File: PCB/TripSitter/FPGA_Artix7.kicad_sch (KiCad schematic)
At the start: 31 parts, among them U1 XC7A100T-FGG484, U3 IS62WVS2568FBLL-20NLI

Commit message: attempt at routing
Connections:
- now unconnected: U1.A13 (IO_L10P_T1_16), U1.A14 (IO_L10N_T1_16), U1.A15 (IO_L9P_T1_DQS_16), U1.A16 (IO_L9N_T1_DQS_16), U1.A18 (IO_L17P_T2_16), U1.A19 (IO_L17N_T2_16), U1.A20 (IO_L16N_T2_16), U1.A21 (IO_L21N_T3_DQS_16), U1.B13 (IO_L8N_T1_16), U1.B15 (IO_L7P_T1_16), U1.B16 (IO_L7N_T1_16), U1.B17 (IO_L11P_T1_SRCC_16), U1.B18 (IO_L11N_T1_SRCC_16), U1.B20 (IO_L16P_T2_16), U1.B21 (IO_L21P_T3_DQS_16), U1.B22 (IO_L20N_T3_16), U1.C13 (IO_L8P_T1_16), U1.C17 (IO_L12N_T1_MRCC_16), U1.C18 (IO_L13P_T2_MRCC_16), U1.C19 (IO_L13N_T2_MRCC_16), U1.C20 (IO_L19N_T3_VREF_16), U1.C22 (IO_L20P_T3_16), U1.D15 (IO_L6N_T0_VREF_16), U1.D17 (IO_L12P_T1_MRCC_16), U1.D19 (IO_L14N_T2_SRCC_16), U1.D20 (IO_L19P_T3_16), U1.D21 (IO_L23N_T3_16), U1.D22 (IO_L22N_T3_16), U1.E18 (IO_L15N_T2_DQS_16), U1.E19 (IO_L14P_T2_SRCC_16), U1.E21 (IO_L23P_T3_16), U1.E22 (IO_L22P_T3_16), U1.F18 (IO_L15P_T2_DQS_16), U1.F19 (IO_L18P_T2_16), U1.F20 (IO_L18N_T2_16), U1.G21 (IO_L24P_T3_16), U1.G22 (IO_L24N_T3_16)
- no-connect marks 52 -> 87

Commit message: before
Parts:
- added J14: Conn_02x10_Counter_Clockwise, Connector_PinHeader_1.00mm:PinHeader_2x10_P1.00mm_Vertical, symbol Connector_Generic:Conn_02x10_Counter_Clockwise
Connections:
- net +3V3 is gone; now on net +3.3V: C28.1, C30.1, C31.1, C32.1, C33.1, C34.1, C35.1, C36.1, C37.1, C38.1, C39.1, C40.1, C41.1, C42.1, C43.1, C44.1, C45.1, C80.1, C81.1, C82.1, C83.1, C87.1, C88.1, C89.1, C90.1, C91.1, C92.1, C93.1, U1.A17 (VCCO_16), U1.AA17 (VCCO_13), U1.AB14 (VCCO_13), U1.B14 (VCCO_16), U1.C21 (VCCO_16), U1.D18 (VCCO_16), U1.E15 (VCCO_16), U1.F22 (VCCO_16), U1.G19 (VCCO_15), U1.H16 (VCCO_15), U1.J13 (VCCO_15), U1.K20 (VCCO_15), U1.L17 (VCCO_15), U1.M14 (VCCO_14), U1.N21 (VCCO_15), U1.P18 (VCCO_14), U1.R15 (VCCO_14), U1.T22 (VCCO_14), U1.U19 (VCCO_14), U1.V16 (VCCO_13), U1.W13 (VCCO_13), U1.Y10 (VCCO_13), U1.Y20 (VCCO_14)
- net at U1.AA10 (IO_L9P_T1_DQS_13): now also J14.7 (Pin_7)
- net at U1.AA11 (IO_L9N_T1_DQS_13): now also J14.8 (Pin_8)
- net at U1.AA9 (IO_L8P_T1_13): now also J14.5 (Pin_5)
- net at U1.AB10 (IO_L8N_T1_13): now also J14.6 (Pin_6)
- net at U1.AB11 (IO_L7P_T1_13): now also J14.3 (Pin_3)
- net at U1.AB12 (IO_L7N_T1_13): now also J14.4 (Pin_4)
- net FPGA_BANK13_20: now reaches U1.T14 (IO_L15P_T2_DQS_13)
- net FPGA_BANK13_20: now also J14.12 (Pin_12)
- net FPGA_BANK13_21: now reaches U1.T15 (IO_L15N_T2_DQS_13)
- net FPGA_BANK13_21: now also J14.11 (Pin_11)
- net FPGA_BANK13_18: now reaches U1.U15 (IO_L14P_T2_SRCC_13)
- net FPGA_BANK13_18: now also J14.14 (Pin_14)
- net at U1.V10 (IO_L10P_T1_13): now also J14.9 (Pin_9)
- net FPGA_BANK13_16: now reaches U1.V13 (IO_L13P_T2_MRCC_13)
- net FPGA_BANK13_16: now also J14.16 (Pin_16)
- net FPGA_BANK13_17: now reaches U1.V14 (IO_L13N_T2_MRCC_13)
- net FPGA_BANK13_17: now also J14.15 (Pin_15)
- net FPGA_BANK13_19: now reaches U1.V15 (IO_L14N_T2_SRCC_13)
- net FPGA_BANK13_19: now also J14.13 (Pin_13)
- net at U1.W10 (IO_L10N_T1_13): now also J14.10 (Pin_10)
- net FPGA_BANK13_15: now reaches U1.W11 (IO_L12P_T1_MRCC_13)
- net FPGA_BANK13_15: now also U1.W12 (IO_L12N_T1_MRCC_13), J14.17 (Pin_17), J14.18 (Pin_18)
- net at U1.W14 (IO_L6P_T0_13): now also J14.1 (Pin_1)
- net FPGA_BANK13_13: now reaches U1.Y11 (IO_L11P_T1_SRCC_13)
- net FPGA_BANK13_13: now also J14.20 (Pin_20)
- net FPGA_BANK13_14: now reaches U1.Y12 (IO_L11N_T1_SRCC_13)
- net FPGA_BANK13_14: now also J14.19 (Pin_19)
- net at U1.Y14 (IO_L6N_T0_VREF_13): now also J14.2 (Pin_2)
- net MCU_PE7: now reaches U1.L15 (IO_L22N_T3_A16_15)
- net EBI_A0: no longer names the net of U1.J16 (IO_0_15)
- net EBI_A1: no longer names the net of U1.H13 (IO_L1P_T0_AD0P_15)
- net EBI_A10: no longer names the net of U1.H15 (IO_L5N_T0_AD9N_15)
- net EBI_A11: no longer names the net of U1.H17 (IO_L6P_T0_15)
- net EBI_A12: no longer names the net of U1.H18 (IO_L6N_T0_VREF_15)
- net EBI_A13: no longer names the net of U1.J22 (IO_L7P_T1_AD2P_15)
- net EBI_A14: no longer names the net of U1.H22 (IO_L7N_T1_AD2N_15)
- net EBI_A15: no longer names the net of U1.H20 (IO_L8P_T1_AD10P_15)
- net EBI_A16: no longer names the net of U1.G20 (IO_L8N_T1_AD10N_15)
- net EBI_A17: no longer names the net of U1.K21 (IO_L9P_T1_DQS_AD3P_15)
- net EBI_A18: no longer names the net of U1.K22 (IO_L9N_T1_DQS_AD3N_15)
- net EBI_A19: no longer names the net of U1.M21 (IO_L10P_T1_AD11P_15)
- net EBI_A2: no longer names the net of U1.G13 (IO_L1N_T0_AD0N_15)
- net EBI_A20: no longer names the net of U1.L21 (IO_L10N_T1_AD11N_15)
- net EBI_A21: no longer names the net of U1.J20 (IO_L11P_T1_SRCC_15)
- net EBI_A22: no longer names the net of U1.J21 (IO_L11N_T1_SRCC_15)
- net EBI_A23: no longer names the net of U1.J19 (IO_L12P_T1_MRCC_15)
- net EBI_A24: no longer names the net of U1.H19 (IO_L12N_T1_MRCC_15)
- net EBI_A25: no longer names the net of U1.K18 (IO_L13P_T2_MRCC_15)
- net EBI_A26: no longer names the net of U1.K19 (IO_L13N_T2_MRCC_15)
- net EBI_A27: no longer names the net of U1.L19 (IO_L14P_T2_SRCC_15)
- net EBI_A3: no longer names the net of U1.G15 (IO_L2P_T0_AD8P_15)
- net EBI_A4: no longer names the net of U1.G16 (IO_L2N_T0_AD8N_15)
- net EBI_A5: no longer names the net of U1.J14 (IO_L3P_T0_DQS_AD1P_15)
- net EBI_A6: no longer names the net of U1.H14 (IO_L3N_T0_DQS_AD1N_15)
- net EBI_A7: no longer names the net of U1.G17 (IO_L4P_T0_15)
- net EBI_A8: no longer names the net of U1.G18 (IO_L4N_T0_15)
- net EBI_A9: no longer names the net of U1.J15 (IO_L5P_T0_AD9P_15)
- net EBI_AD0: no longer names the net of U1.L20 (IO_L14N_T2_SRCC_15)
- net EBI_AD1: no longer names the net of U1.N22 (IO_L15P_T2_DQS_15)
- net EBI_AD10: no longer names the net of U1.K14 (IO_L19N_T3_A21_VREF_15)
- net EBI_AD11: no longer names the net of U1.M13 (IO_L20P_T3_A20_15)
- net EBI_AD12: no longer names the net of U1.L13 (IO_L20N_T3_A19_15)
- net EBI_AD13: no longer names the net of U1.K17 (IO_L21P_T3_DQS_15)
- net EBI_AD14: no longer names the net of U1.J17 (IO_L21N_T3_DQS_A18_15)
- net EBI_AD15: no longer names the net of U1.L14 (IO_L22P_T3_A17_15)
- net EBI_AD2: no longer names the net of U1.M22 (IO_L15N_T2_DQS_ADV_B_15)
- net EBI_AD3: no longer names the net of U1.M18 (IO_L16P_T2_A28_15)
- net EBI_AD4: no longer names the net of U1.L18 (IO_L16N_T2_A27_15)
- net EBI_AD5: no longer names the net of U1.N18 (IO_L17P_T2_A26_15)
- net EBI_AD6: no longer names the net of U1.N19 (IO_L17N_T2_A25_15)
- net EBI_AD7: no longer names the net of U1.N20 (IO_L18P_T2_A24_15)
- net EBI_AD8: no longer names the net of U1.M20 (IO_L18N_T2_A23_15)
- net EBI_AD9: no longer names the net of U1.K13 (IO_L19P_T3_A22_15)
- net EBI_ALE renamed MCU_PE8
- net EBI_ARDY: no longer names the net of U1.F21 (IO_25_16)
- net EBI_BL0: no longer names the net of U1.M16 (IO_L24N_T3_RS0_15)
- net EBI_BL1: no longer names the net of U1.M17 (IO_25_15)
- net EBI_REn renamed MCU_PE9
- net EBI_WEn renamed MCU_PE10
- net HDMI_CLKN renamed HDMI_TX0_N
- net HDMI_CLKP renamed HDMI_TX0_P
- net HDMI_TX0N renamed HDMI_CLK_N
- net HDMI_TX0P renamed HDMI_CLK_P
- net HDMI_TX1N renamed HDMI_TX1_N
- net HDMI_TX1P renamed HDMI_TX1_P
- net HDMI_TX2N renamed HDMI_TX2_N
- net HDMI_TX2P renamed HDMI_TX2_P
- no-connect marks 87 -> 113

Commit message: more pcb routing
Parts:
- removed C87: 47uF, Capacitor_SMD:C_1210_3225Metric_Pad1.33x2.70mm_HandSolder, symbol Device:C
- removed C88, C89: 4.7uF, Capacitor_SMD:C_0805_2012Metric_Pad1.18x1.45mm_HandSolder, symbol Device:C
- removed C90, C91, C92, C93: 470nF, Capacitor_SMD:C_0201_0603Metric_Pad0.64x0.40mm_HandSolder, symbol Device:C
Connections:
- net +3.3V: no longer U1.G19 (VCCO_15), U1.H16 (VCCO_15), U1.J13 (VCCO_15), U1.K20 (VCCO_15), U1.L17 (VCCO_15), U1.N21 (VCCO_15)
- net HDMI_CEC: now also U1.B21 (IO_L21P_T3_DQS_16); no longer U1.D14 (IO_L6P_T0_16)
- net HDMI_CLK_N: now also U1.G22 (IO_L24N_T3_16); no longer U1.E14 (IO_L4N_T0_16)
- net HDMI_CLK_P: now also U1.G21 (IO_L24P_T3_16); no longer U1.E13 (IO_L4P_T0_16)
- net HDMI_HPD: now also U1.F19 (IO_L18P_T2_16); no longer U1.F15 (IO_0_16)
- net HDMI_SCL: now also U1.D20 (IO_L19P_T3_16); no longer U1.E16 (IO_L5P_T0_16)
- net HDMI_SDA: now also U1.F20 (IO_L18N_T2_16); no longer U1.D16 (IO_L5N_T0_16)
- net HDMI_TX0_N: now also U1.E22 (IO_L22P_T3_16); no longer U1.C15 (IO_L3N_T0_DQS_16)
- net HDMI_TX0_P: now also U1.D22 (IO_L22N_T3_16); no longer U1.C14 (IO_L3P_T0_DQS_16)
- net HDMI_TX1_N: now also U1.C22 (IO_L20P_T3_16); no longer U1.E17 (IO_L2N_T0_16)
- net HDMI_TX1_P: now also U1.B22 (IO_L20N_T3_16); no longer U1.F16 (IO_L2P_T0_16)
- net HDMI_TX2_N: now also U1.A21 (IO_L21N_T3_DQS_16); no longer U1.F14 (IO_L1N_T0_16)
- net HDMI_TX2_P: now also U1.A20 (IO_L16N_T2_16); no longer U1.F13 (IO_L1P_T0_16)
- net MCU_PE10: now also U1.U16 (IO_L17N_T2_13); no longer U1.M15 (IO_L24P_T3_RS1_15)
- net MCU_PE7: now also U1.W15 (IO_L16P_T2_13); no longer U1.L15 (IO_L22N_T3_A16_15)
- net MCU_PE8: now also U1.W16 (IO_L16N_T2_13); no longer U1.L16 (IO_L23P_T3_FOE_B_15)
- net MCU_PE9: now also U1.T16 (IO_L17P_T2_13); no longer U1.K16 (IO_L23N_T3_FWE_B_15)
- net QSPI0_DQ0: now also U1.B17 (IO_L11P_T1_SRCC_16); no longer U1.W22 (IO_L7N_T1_D10_14), U1.Y16 (IO_L1P_T0_13), U3.5 (SIO0)
- net QSPI0_DQ1: now also U1.B18 (IO_L11N_T1_SRCC_16); no longer U1.AA16 (IO_L1N_T0_13), U1.AA20 (IO_L8P_T1_D11_14), U3.2 (SIO1)
- net QSPI0_DQ2: now also U1.A18 (IO_L17P_T2_16); no longer U1.AA21 (IO_L8N_T1_D12_14), U1.AB16 (IO_L2P_T0_13), U3.3 (SIO2)
- net QSPI0_DQ3: now also U1.A19 (IO_L17N_T2_16); no longer U1.AB17 (IO_L2N_T0_13), U1.Y21 (IO_L9P_T1_DQS_14), U3.7 (SIO3)
- net QSPI0_DQ4: now also U1.A16 (IO_L9N_T1_DQS_16); no longer U1.AA15 (IO_L4P_T0_13)
- net QSPI0_DQ5: now also U1.C17 (IO_L12N_T1_MRCC_16); no longer U1.AB15 (IO_L4N_T0_13)
- net QSPI0_DQ6: now also U1.A15 (IO_L9P_T1_DQS_16); no longer U1.Y13 (IO_L5P_T0_13)
- net QSPI0_DQ7: now also U1.C18 (IO_L13P_T2_MRCC_16); no longer U1.AA14 (IO_L5N_T0_13)
- net QSPI_CS: now also U1.B15 (IO_L7P_T1_16); no longer U1.Y17 (IO_0_13)
- net QSPI_DQS: now also U1.D17 (IO_L12P_T1_MRCC_16); no longer U1.AA13 (IO_L3P_T0_DQS_13)
- net QSPI_SCLK: now also U1.D14 (IO_L6P_T0_16); no longer U1.AB13 (IO_L3N_T0_DQS_13)
- net VGA_B3: now reaches U1.AB20 (IO_L15N_T2_DQS_DOUT_CSO_B_14)
- net VGA_B1: now reaches U1.AB21 (IO_L10P_T1_D14_14)
- net VGA_B0: now reaches U1.AB22 (IO_L10N_T1_D15_14)
- net VGA_HSync: now reaches U1.U22 (IO_L3P_T0_DQS_PUDC_B_14)
- net VGA_G2: now reaches U1.V18 (IO_L14P_T2_SRCC_14)
- net VGA_VSync: now reaches U1.V22 (IO_L3N_T0_DQS_EMCCLK_14)
- net VGA_G3: now reaches U1.Y18 (IO_L13P_T2_MRCC_14)
- net QSPI0_CS0 renamed SRAM_QSPI0_CS0
- net SRAM_QSPI0_CS0: no longer U1.W21 (IO_L7P_T1_D09_14)
- net QSPI0_SCLK renamed SRAM_QSPI0_SCLK
- net SRAM_QSPI0_SCLK: no longer U1.Y22 (IO_L9N_T1_DQS_D13_14)
- net VGA connector/VGA_B0: no longer names the net of U1.R18 (IO_L20P_T3_A08_D24_14)
- net VGA connector/VGA_B1: no longer names the net of U1.T18 (IO_L20N_T3_A07_D23_14)
- net VGA connector/VGA_B2: no longer names the net of U1.N17 (IO_L21P_T3_DQS_14)
- net VGA connector/VGA_B3: no longer names the net of U1.P17 (IO_L21N_T3_DQS_A06_D22_14)
- net VGA connector/VGA_G0: no longer names the net of U1.U17 (IO_L18P_T2_A12_D28_14)
- net VGA connector/VGA_G1: no longer names the net of U1.U18 (IO_L18N_T2_A11_D27_14)
- net VGA connector/VGA_G2: no longer names the net of U1.P14 (IO_L19P_T3_A10_D26_14)
- net VGA connector/VGA_G3: no longer names the net of U1.R14 (IO_L19N_T3_A09_D25_VREF_14)
- net VGA connector/VGA_HSync: no longer names the net of U1.P15 (IO_L22P_T3_A05_D21_14)
- net VGA connector/VGA_R0: no longer names the net of U1.V17 (IO_L16P_T2_CSI_B_14)
- net VGA connector/VGA_R1: no longer names the net of U1.W17 (IO_L16N_T2_A15_D31_14)
- net VGA connector/VGA_R2: no longer names the net of U1.AA18 (IO_L17P_T2_A14_D30_14)
- net VGA connector/VGA_R3: no longer names the net of U1.AB18 (IO_L17N_T2_A13_D29_14)
- net VGA connector/VGA_VSync: no longer names the net of U1.R16 (IO_L22N_T3_A04_D20_14)
- new net SRAM_QSPI0_DQ0: U3.5 (SIO0)
- new net SRAM_QSPI0_DQ1: U3.2 (SIO1)
- new net SRAM_QSPI0_DQ2: U3.3 (SIO2)
- new net SRAM_QSPI0_DQ3: U3.7 (SIO3)
- new net VGA_B2: U1.AA20 (IO_L8P_T1_D11_14)
- new net VGA_G0: U1.AA21 (IO_L8N_T1_D12_14)
- new net VGA_R0: U1.W22 (IO_L7N_T1_D10_14)
- new net VGA_R1: U1.W21 (IO_L7P_T1_D09_14)
- new net VGA_R2: U1.Y22 (IO_L9N_T1_DQS_D13_14)
- new net VGA_R3: U1.Y21 (IO_L9P_T1_DQS_14)
- no-connect marks 113 -> 112

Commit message: pcb: Finalized routing without DDR3
Added ground and power plane, layed out all the components, fanned out
BGA. QSPI between FPGA->MCU->SRAM and MCU->SRAM is routed. Most is done
but DRC does not pass so do not produce.
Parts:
- removed C34: 4.7uF, Capacitor_SMD:C_0805_2012Metric_Pad1.18x1.45mm_HandSolder, symbol Device:C
- removed J14: Conn_02x10_Counter_Clockwise, Connector_PinHeader_1.00mm:PinHeader_2x10_P1.00mm_Vertical, symbol Connector_Generic:Conn_02x10_Counter_Clockwise
- added C1: 0.1uF, Capacitor_SMD:C_0603_1608Metric_Pad1.08x0.95mm_HandSolder, symbol Device:C
- added C13, C14, C15, C25, C26, C27: 470nF, Capacitor_SMD:C_0402_1005Metric_Pad0.74x0.62mm_HandSolder, symbol Device:C
- added C2, C52, C53, C54, C55, C56, C57, C58: 470nF, Capacitor_SMD:C_0201_0603Metric_Pad0.64x0.40mm_HandSolder, symbol Device:C
- added C29: 4.7uF, Capacitor_SMD:C_0402_1005Metric_Pad0.74x0.62mm_HandSolder, symbol Device:C
- added C34: 330uF, Capacitor_Tantalum_SMD:CP_EIA-7343-43_Kemet-X_Pad2.25x2.55mm_HandSolder, symbol T520V337M2R5ATE025:T520V337M2R5ATE025
- added C46, C47, C48, C49, C50: 4.7uF, Capacitor_SMD:C_0201_0603Metric_Pad0.64x0.40mm_HandSolder, symbol Device:C
- added unit 7 of U1
- added U4: DSC1001DL5-100.0000T, Footprints:CDFN4_2P5X2_MCH-L, symbol DSC1001DL5-100-0000T:DSC1001DL5-100.0000T
- C28, C31: value 470nF -> 4.7uF; footprint Capacitor_SMD:C_0201_0603Metric_Pad0.64x0.40mm_HandSolder -> Capacitor_SMD:C_0402_1005Metric_Pad0.74x0.62mm_HandSolder; Component name GRM188R71C474KA88D -> CL05A475KQ5NRNC; DK_Detail_Page https://www.digikey.no/product-detail/en/murata-electronics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 -> https://www.digikey.no/no/products/detail/samsung-electro-m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
- C30: footprint Capacitor_SMD:C_0201_0603Metric_Pad0.64x0.40mm_HandSolder -> Capacitor_SMD:C_0402_1005Metric_Pad0.74x0.62mm_HandSolder
- C32: value 470nF -> 47uF; footprint Capacitor_SMD:C_0201_0603Metric_Pad0.64x0.40mm_HandSolder -> Capacitor_SMD:C_0603_1608Metric_Pad1.08x0.95mm_HandSolder; Component name GRM188R71C474KA88D -> CL10A476MR8NZNE; DK_Detail_Page https://www.digikey.no/product-detail/en/murata-electronics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 -> https://www.digikey.no/no/products/detail/samsung-electro-m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
- C33: value 4.7uF -> 100uF; Component name C2012X7R1A475K125AC -> GRM21BR60G107ME11L; DK_Detail_Page https://www.digikey.no/product-detail/no/tdk-corporation/C2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 -> https://www.digikey.no/en/products/detail/murata-electronic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
- C35: value 47uF -> 4.7uF; footprint Capacitor_SMD:C_1210_3225Metric_Pad1.33x2.70mm_HandSolder -> Capacitor_SMD:C_0201_0603Metric_Pad0.64x0.40mm_HandSolder; Component name GRM32ER71A476ME15L -> CL03A475MQ5C65C; DK_Detail_Page https://www.digikey.no/product-detail/no/murata-electronics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 -> https://www.digikey.no/no/products/detail/samsung-electro-m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
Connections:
- net SRAM_QSPI0_DQ0 is gone; now on net QSPI0_DQ0: U3.5 (SIO0)
- net SRAM_QSPI0_DQ1 is gone; now on net QSPI0_DQ1: U3.2 (SIO1)
- net SRAM_QSPI0_DQ2 is gone; now on net QSPI0_DQ2: U3.3 (SIO2)
- net SRAM_QSPI0_DQ3 is gone; now on net QSPI0_DQ3: U3.7 (SIO3)
- net SRAM_QSPI0_SCLK is gone; now on net QSPI_SCLK: U3.6 (SCK)
- net +3.3V: now also C1.2, U4.1 (*STANDBY), U4.4 (VDD); no longer C28.1, C30.1, C31.1, C32.1, C33.1, C35.1, U1.AA17 (VCCO_13), U1.AB14 (VCCO_13), U1.V16 (VCCO_13), U1.W13 (VCCO_13), U1.Y10 (VCCO_13)
- net GND: now also C1.1, C13.2, C14.2, C15.2, C2.2, C25.2, C26.2, C27.2, C29.2, C34.1, C46.2, C47.2, C48.2, C49.2, C50.2, C52.2, C53.2, C54.2, C55.2, C56.2, C57.2, C58.2, U1.A11 (GND), U1.A12 (GND), U1.A2 (GND), U1.A22 (GND), U1.A3 (GND), U1.A5 (GND), U1.A7 (GND), U1.A9 (GND), U1.AA12 (GND), U1.AA2 (GND), U1.AA22 (GND), U1.AB19 (GND), U1.AB9 (GND), U1.B12 (GND), U1.B19 (GND), U1.B3 (GND), U1.C10 (GND), U1.C12 (GND), U1.C16 (GND), U1.C3 (GND), U1.C6 (GND), U1.D12 (GND), U1.D13 (GND), U1.D3 (GND), U1.D4 (GND), U1.D8 (GND), U1.E11 (GND), U1.E12 (VCCBATT_0), U1.E20 (GND), U1.E4 (GND), U1.E5 (GND), U1.E7 (GND), U1.E9 (GND), U1.F11 (GND), U1.F17 (GND), U1.F5 (GND), U1.G10 (GND), U1.G12 (GND), U1.G14 (GND), U1.G5 (GND), U1.G6 (GND), U1.G7 (GND), U1.G8 (GND), U1.G9 (GND), U1.H1 (GND), U1.H11 (GND), U1.H21 (GND), U1.H7 (GND), U1.H9 (GND), U1.J10 (GND), U1.J12 (GND), U1.J18 (GND), U1.J8 (GND), U1.K11 (GND), U1.K15 (GND), U1.K5 (GND), U1.K7 (GND), U1.K9 (GNDADC_0), U1.L2 (GND), U1.L22 (GND), U1.L8 (GND), U1.M11 (GND), U1.M19 (GND), U1.M7 (GND), U1.N16 (GND), U1.N6 (GND), U1.N8 (GND), U1.P11 (GND), U1.P13 (GND), U1.P3 (GND), U1.P7 (GND), U1.P9 (GND), U1.R10 (GND), U1.R12 (GND), U1.R20 (GND), U1.R8 (GND), U1.T11 (GND), U1.T17 (GND), U1.T7 (GND), U1.T9 (GND), U1.U14 (GND), U1.U4 (GND), U1.V1 (GND), U1.V11 (GND), U1.V21 (GND), U1.W18 (GND), U1.W8 (GND), U1.Y15 (GND), U1.Y5 (GND), U4.2 (GND)
- net HDMI_CLK_N: now also U1.G21 (IO_L24P_T3_16); no longer U1.G22 (IO_L24N_T3_16)
- net HDMI_CLK_P: now also U1.G22 (IO_L24N_T3_16); no longer U1.G21 (IO_L24P_T3_16)
- net MCU_PE7: now also U1.A13 (IO_L10P_T1_16); no longer U1.W15 (IO_L16P_T2_13)
- net MCU_PE8: now also U1.A14 (IO_L10N_T1_16), U1.C15 (IO_L3N_T0_DQS_16); no longer U1.W16 (IO_L16N_T2_13)
- net MCU_PE9: now also U1.F16 (IO_L2P_T0_16); no longer U1.T16 (IO_L17P_T2_13)
- net SRAM_QSPI0_CS0: now also U1.C19 (IO_L13N_T2_MRCC_16)
- net VGA_B0: now also U1.AB20 (IO_L15N_T2_DQS_DOUT_CSO_B_14); no longer U1.AB22 (IO_L10N_T1_D15_14)
- net VGA_B1: now also U1.AA19 (IO_L15P_T2_DQS_RDWR_B_14); no longer U1.AB21 (IO_L10P_T1_D14_14)
- net VGA_B2: now also U1.AA18 (IO_L17P_T2_A14_D30_14); no longer U1.AA20 (IO_L8P_T1_D11_14)
- net VGA_B3: now also U1.AB18 (IO_L17N_T2_A13_D29_14); no longer U1.AB20 (IO_L15N_T2_DQS_DOUT_CSO_B_14)
- net VGA_G0: now also U1.AB22 (IO_L10N_T1_D15_14); no longer U1.AA21 (IO_L8N_T1_D12_14)
- net VGA_G1: now also U1.AA21 (IO_L8N_T1_D12_14)
- net VGA_G2: now also U1.AB21 (IO_L10P_T1_D14_14); no longer U1.V18 (IO_L14P_T2_SRCC_14)
- net VGA_G3: now also U1.AA20 (IO_L8P_T1_D11_14); no longer U1.Y18 (IO_L13P_T2_MRCC_14)
- net GCLK100: now reaches U1.W20 (IO_L12N_T1_MRCC_14)
- net GCLK100: now also U4.3 (OUT)
- net FPGA_BANK13_13: no longer names the net of U1.Y11 (IO_L11P_T1_SRCC_13)
- net FPGA_BANK13_14: no longer names the net of U1.Y12 (IO_L11N_T1_SRCC_13)
- net FPGA_BANK13_15: no longer names the net of U1.W11 (IO_L12P_T1_MRCC_13)
- net FPGA_BANK13_15: no longer U1.W12 (IO_L12N_T1_MRCC_13)
- net FPGA_BANK13_16: no longer names the net of U1.V13 (IO_L13P_T2_MRCC_13)
- net FPGA_BANK13_17: no longer names the net of U1.V14 (IO_L13N_T2_MRCC_13)
- net FPGA_BANK13_18: no longer names the net of U1.U15 (IO_L14P_T2_SRCC_13)
- net FPGA_BANK13_19: no longer names the net of U1.V15 (IO_L14N_T2_SRCC_13)
- net FPGA_BANK13_20: no longer names the net of U1.T14 (IO_L15P_T2_DQS_13)
- net FPGA_BANK13_21: no longer names the net of U1.T15 (IO_L15N_T2_DQS_13)
- net MCU_PE10: no longer names the net of U1.U16 (IO_L17N_T2_13)
- new net +1V0: C2.1, C27.1, C30.1, C33.1, C34.2, C35.1, C46.1, C47.1, C48.1, C49.1, C50.1, C52.1, C53.1, C54.1, C55.1, C56.1, C57.1, C58.1, U1.H10 (VCCINT), U1.H8 (VCCINT), U1.J11 (VCCBRAM), U1.J7 (VCCINT), U1.J9 (VCCINT), U1.K8 (VCCINT), U1.L11 (VCCBRAM), U1.L7 (VCCINT), U1.M8 (VCCINT), U1.N11 (VCCBRAM), U1.N7 (VCCINT), U1.P10 (VCCINT), U1.P8 (VCCINT), U1.R7 (VCCINT), U1.R9 (VCCINT), U1.T10 (VCCINT), U1.T8 (VCCINT)
- new net +1V8: C13.1, C14.1, C15.1, C25.1, C26.1, C28.1, C29.1, C31.1, C32.1, U1.H12 (VCCAUX), U1.K10 (VCCADC_0), U1.K12 (VCCAUX), U1.M12 (VCCAUX), U1.P12 (VCCAUX), U1.R11 (VCCAUX)
- no-connect marks 112 -> 148
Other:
- removed sheet FPGA Power Block
- note added: "Correct"
- moved on the sheet: C100, C36, C37, C38, C39, C40, C41, C42, C43, C44, C45, C80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

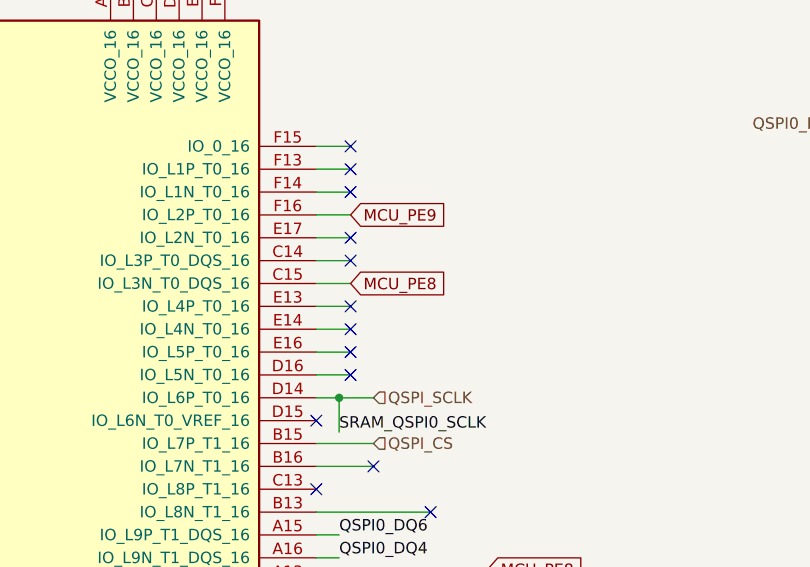
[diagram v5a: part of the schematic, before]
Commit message: fix DRC errors and edit footprint vias
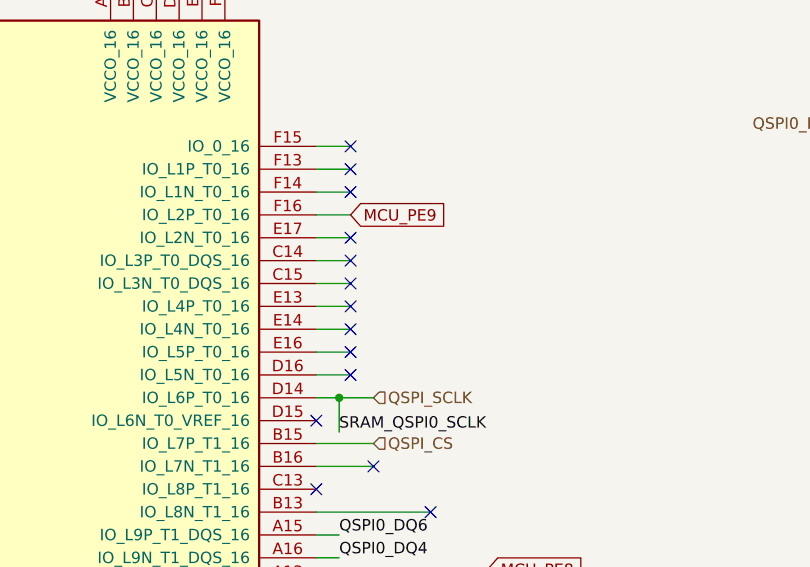
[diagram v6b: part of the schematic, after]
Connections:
- net MCU_PE8: no longer U1.C15 (IO_L3N_T0_DQS_16)
- no-connect marks 148 -> 149
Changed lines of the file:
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@@
   (no_connect (at 439.42 124.46))
   (no_connect (at 121.92 143.51))
+  (no_connect (at 227.33 85.09))
   (no_connect (at 337.82 83.82))
   (no_connect (at 113.03 77.47))
@@
       (effects (font (size 1.27 1.27)) (justify left) hide)
     )
-  )
-  (global_label "MCU_PE8" (shape input) (at 227.33 85.09 0) (fields_autoplaced)
-    (effects (font (size 1.27 1.27)) (justify left))
-    (property "Intersheetrefs" "${INTERSHEET_REFS}" (at 238.9632 85.09 0)
-      (effects (font (size 1.27 1.27)) (justify left) hide)
-    )
